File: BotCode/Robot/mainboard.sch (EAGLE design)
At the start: 18 parts

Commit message: UI improvements
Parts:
- renumbered HMC5883L_0 to HMC5883L, HMV5883L_1 to L3GD20H_LSM303
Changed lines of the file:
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@@
 <part name="GND6" library="SparkFun-Aesthetics" deviceset="GND" device=""/>
 <part name="GND7" library="SparkFun-Aesthetics" deviceset="GND" device=""/>
-<part name="HMV5883L_1" library="SparkFun-Connectors" deviceset="M04" device="PTH"/>
-<part name="HMC5883L_0" library="SparkFun-Connectors" deviceset="M04" device="PTH"/>
+<part name="L3GD20H_LSM303" library="SparkFun-Connectors" deviceset="M04" device="PTH"/>
+<part name="HMC5883L" library="SparkFun-Connectors" deviceset="M04" device="PTH"/>
 <part name="REGULATOR" library="LD1117V33" deviceset="LD1117V33" device=""/>
 <part name="LED_DRIVER" library="BillPorter" deviceset="TLC5916/17" device="DIP-16"/>
@@
 <instance part="GND6" gate="1" x="86.36" y="20.32"/>
 <instance part="GND7" gate="1" x="86.36" y="43.18"/>
-<instance part="HMV5883L_1" gate="G$1" x="119.38" y="58.42"/>
-<instance part="HMC5883L_0" gate="G$1" x="119.38" y="88.9"/>
+<instance part="L3GD20H_LSM303" gate="G$1" x="119.38" y="58.42"/>
+<instance part="HMC5883L" gate="G$1" x="119.38" y="88.9"/>
 <instance part="REGULATOR" gate="G$1" x="134.62" y="154.94"/>
 <instance part="LED_DRIVER" gate="G$1" x="88.9" y="109.22" rot="R180"/>
@@
 </segment>
 <segment>
-<pinref part="HMV5883L_1" gate="G$1" pin="2"/>
+<pinref part="L3GD20H_LSM303" gate="G$1" pin="2"/>
 <wire x1="124.46" y1="58.42" x2="132.08" y2="58.42" width="0.1524" layer="91"/>
 <pinref part="C2" gate="G$1" pin="1"/>
@@
 </segment>
 <segment>
-<pinref part="HMC5883L_0" gate="G$1" pin="2"/>
+<pinref part="HMC5883L" gate="G$1" pin="2"/>
 <wire x1="124.46" y1="88.9" x2="132.08" y2="88.9" width="0.1524" layer="91"/>
 <pinref part="C3" gate="G$1" pin="1"/>
@@
 <wire x1="149.86" y1="81.28" x2="144.78" y2="81.28" width="0.1524" layer="91"/>
 <wire x1="144.78" y1="81.28" x2="144.78" y2="93.98" width="0.1524" layer="91"/>
-<pinref part="HMC5883L_0" gate="G$1" pin="4"/>
+<pinref part="HMC5883L" gate="G$1" pin="4"/>
 <wire x1="144.78" y1="93.98" x2="124.46" y2="93.98" width="0.1524" layer="91"/>
 </segment>
@@
 <net name="N$17" class="0">
 <segment>
-<pinref part="HMC5883L_0" gate="G$1" pin="3"/>
+<pinref part="HMC5883L" gate="G$1" pin="3"/>
 <wire x1="124.46" y1="91.44" x2="142.24" y2="91.44" width="0.1524" layer="91"/>
 <wire x1="142.24" y1="91.44" x2="142.24" y2="78.74" width="0.1524" layer="91"/>
@@
 <wire x1="149.86" y1="68.58" x2="142.24" y2="68.58" width="0.1524" layer="91"/>
 <wire x1="142.24" y1="68.58" x2="142.24" y2="63.5" width="0.1524" layer="91"/>
-<pinref part="HMV5883L_1" gate="G$1" pin="4"/>
+<pinref part="L3GD20H_LSM303" gate="G$1" pin="4"/>
 <wire x1="142.24" y1="63.5" x2="124.46" y2="63.5" width="0.1524" layer="91"/>
 </segment>
@@
 <net name="N$21" class="0">
 <segment>
-<pinref part="HMV5883L_1" gate="G$1" pin="3"/>
+<pinref part="L3GD20H_LSM303" gate="G$1" pin="3"/>
 <wire x1="124.46" y1="60.96" x2="137.16" y2="60.96" width="0.1524" layer="91"/>
 <wire x1="137.16" y1="60.96" x2="137.16" y2="71.12" width="0.1524" layer="91"/>
@@
 </segment>
 <segment>
-<pinref part="HMV5883L_1" gate="G$1" pin="1"/>
+<pinref part="L3GD20H_LSM303" gate="G$1" pin="1"/>
 <wire x1="124.46" y1="55.88" x2="127" y2="55.88" width="0.1524" layer="91"/>
 <wire x1="127" y1="55.88" x2="127" y2="48.26" width="0.1524" layer="91"/>
@@
 </segment>
 <segment>
-<pinref part="HMC5883L_0" gate="G$1" pin="1"/>
+<pinref part="HMC5883L" gate="G$1" pin="1"/>
 <wire x1="124.46" y1="86.36" x2="127" y2="86.36" width="0.1524" layer="91"/>
 <wire x1="127" y1="86.36" x2="127" y2="78.74" width="0.1524" layer="91"/>

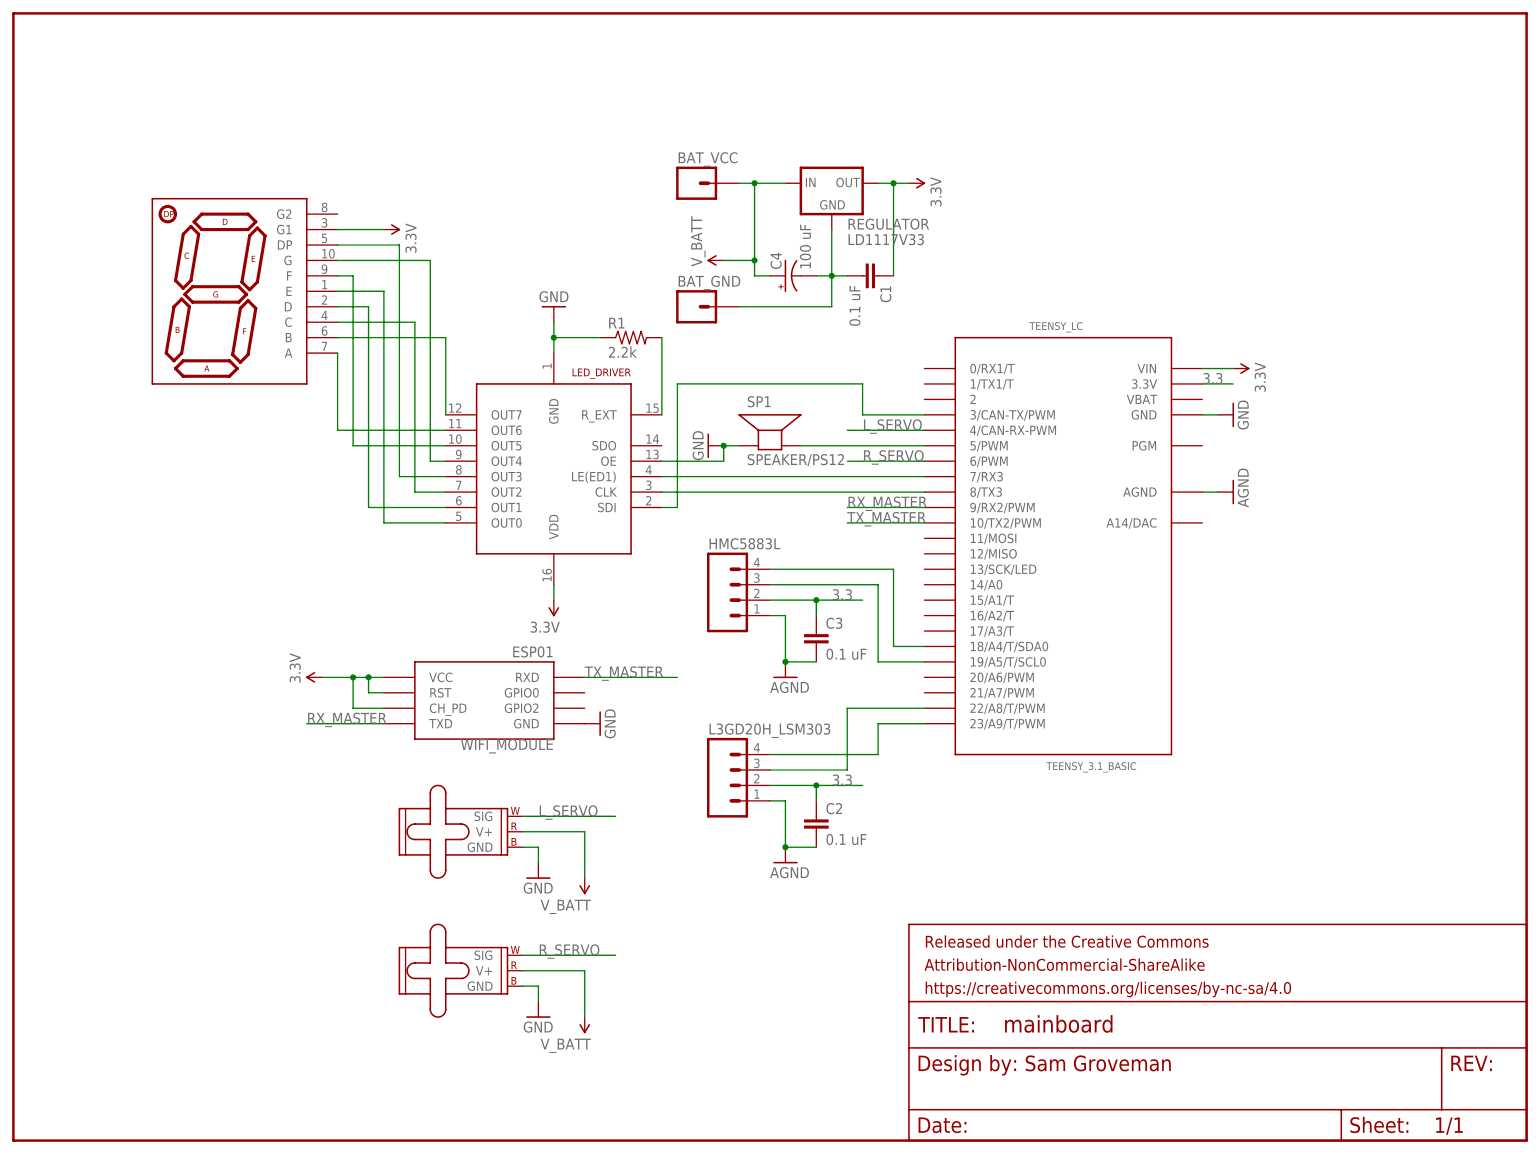
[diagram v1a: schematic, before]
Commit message: Added initial support for robot tuning.
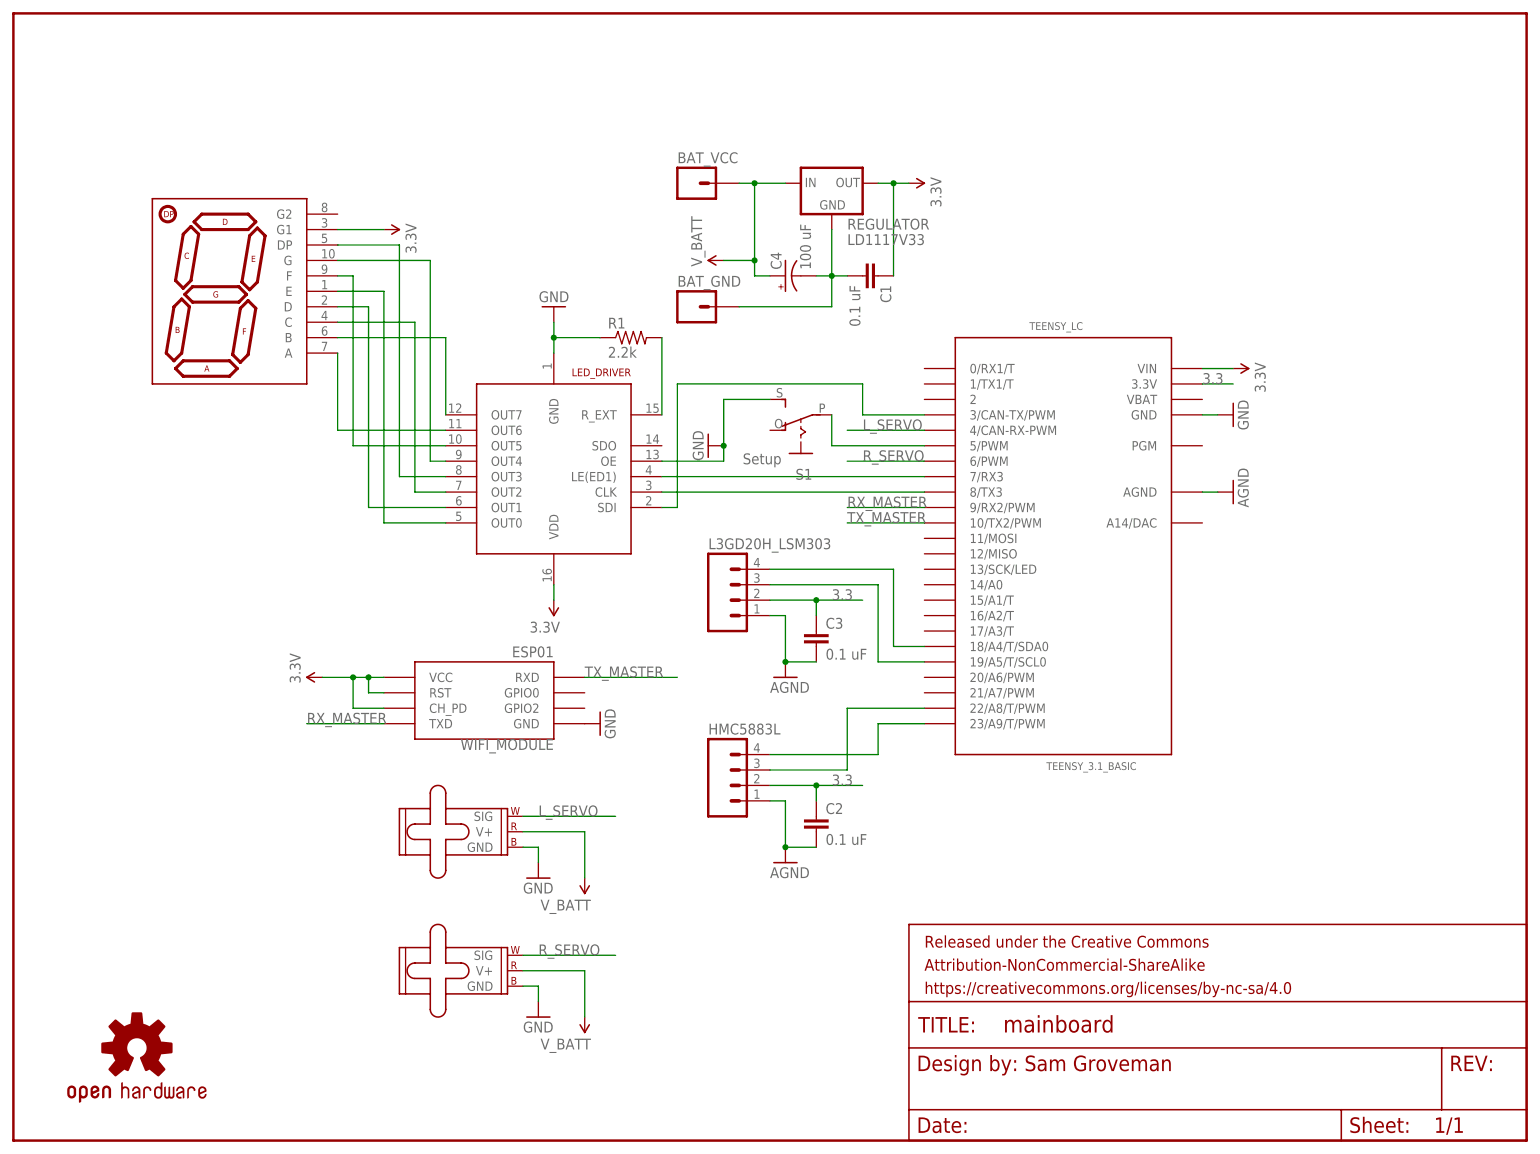
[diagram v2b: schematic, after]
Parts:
- removed SP1: SPEAKER/PS12, adafruit:SPEAKER/PS12
- added LOGO1: OSHW-LOGOL, SparkFun-Aesthetics:OSHW-LOGOL
- added S1: Setup, adafruit:EG1218S
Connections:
- net N$1 renamed R_EXT
- net N$10 renamed LED_4
- net N$11 renamed LED_9
- net N$12 renamed LED_10
- net N$2 renamed SDI
- net N$3 renamed CLK
- net N$4 renamed LE
- net N$5 renamed LED_5
- net N$6 renamed LED_6
- net N$7 renamed LED_1
- net N$8 renamed LED_2
- net N$9 renamed LED_7
- removed net N$15: SP1.-, TEENSY_LC.5/PWM
- removed net N$16: HMC5883L.4, TEENSY_LC.18/A4/T/SDA0
- removed net N$17: HMC5883L.3, TEENSY_LC.19/A5/T/SCL0
- removed net N$20: L3GD20H_LSM303.4, TEENSY_LC.23/A9/T/PWM
- removed net N$21: L3GD20H_LSM303.3, TEENSY_LC.22/A8/T/PWM
- new net F_SCL: HMC5883L.3, TEENSY_LC.22/A8/T/PWM
- new net F_SDA: HMC5883L.4, TEENSY_LC.23/A9/T/PWM
- new net R_SCL: L3GD20H_LSM303.3, TEENSY_LC.19/A5/T/SCL0
- new net R_SDA: L3GD20H_LSM303.4, TEENSY_LC.18/A4/T/SDA0
- new net SETUP: S1.P, TEENSY_LC.5/PWM
- net GND: now also S1.S; no longer SP1.+
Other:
- moved on the sheet: HMC5883L, L3GD20H_LSM303
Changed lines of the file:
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@@
 <?xml version="1.0" encoding="utf-8"?>
 <!DOCTYPE eagle SYSTEM "eagle.dtd">
-<eagle version="7.4.0">
+<eagle version="7.7.0">
 <drawing>
 <settings>
@@
 <setting verticaltext="up"/>
 </settings>
-<grid distance="0.1" unitdist="inch" unit="inch" style="lines" multiple="1" display="no" altdistance="0.01" altunitdist="inch" altunit="inch"/>
+<grid distance="0.1" unitdist="inch" unit="inch" style="lines" multiple="1" display="yes" altdistance="0.01" altunitdist="inch" altunit="inch"/>
 <layers>
 <layer number="1" name="Top" color="4" fill="1" visible="no" active="no"/>
@@
 <part name="C3" library="SparkFun-Passives" deviceset="CAP" device="PTH" value="0.1 uF"/>
 <part name="C4" library="SparkFun-Passives" deviceset="CAP_POL" device="PTH1" value="100 uF"/>
-<part name="SP1" library="adafruit" deviceset="SPEAKER" device="/PS12"/>
 <part name="R_SERVO" library="SparkFun-Electromechanical" deviceset="SMALL_SERVO" device=""/>
 <part name="L_SERVO" library="SparkFun-Electromechanical" deviceset="SMALL_SERVO" device=""/>
@@
 <part name="GND6" library="SparkFun-Aesthetics" deviceset="GND" device=""/>
 <part name="GND7" library="SparkFun-Aesthetics" deviceset="GND" device=""/>
+<part name="HMC5883L" library="SparkFun-Connectors" deviceset="M04" device="PTH"/>
 <part name="L3GD20H_LSM303" library="SparkFun-Connectors" deviceset="M04" device="PTH"/>
-<part name="HMC5883L" library="SparkFun-Connectors" deviceset="M04" device="PTH"/>
 <part name="REGULATOR" library="LD1117V33" deviceset="LD1117V33" device=""/>
 <part name="LED_DRIVER" library="BillPorter" deviceset="TLC5916/17" device="DIP-16"/>
@@
 <part name="SUPPLY7" library="SparkFun-Aesthetics" deviceset="V_BATT" device=""/>
 <part name="SUPPLY8" library="SparkFun-Aesthetics" deviceset="V_BATT" device=""/>
+<part name="LOGO1" library="SparkFun-Aesthetics" deviceset="OSHW-LOGO" device="L"/>
+<part name="S1" library="adafruit" deviceset="EG1218" device="S" value="Setup"/>
 </parts>
 <sheets>
@@
 <instance part="C3" gate="G$1" x="132.08" y="81.28"/>
 <instance part="C4" gate="G$1" x="127" y="142.24" rot="R90"/>
-<instance part="SP1" gate="S1" x="124.46" y="114.3"/>
 <instance part="R_SERVO" gate="G$1" x="81.28" y="30.48"/>
 <instance part="L_SERVO" gate="G$1" x="81.28" y="53.34"/>
@@
 <instance part="GND6" gate="1" x="86.36" y="20.32"/>
 <instance part="GND7" gate="1" x="86.36" y="43.18"/>
-<instance part="L3GD20H_LSM303" gate="G$1" x="119.38" y="58.42"/>
-<instance part="HMC5883L" gate="G$1" x="119.38" y="88.9"/>
+<instance part="HMC5883L" gate="G$1" x="119.38" y="58.42"/>
+<instance part="L3GD20H_LSM303" gate="G$1" x="119.38" y="88.9"/>
 <instance part="REGULATOR" gate="G$1" x="134.62" y="154.94"/>
 <instance part="LED_DRIVER" gate="G$1" x="88.9" y="109.22" rot="R180"/>
@@
 <instance part="SUPPLY7" gate="G$1" x="93.98" y="43.18" rot="R180"/>
 <instance part="SUPPLY8" gate="G$1" x="93.98" y="20.32" rot="R180"/>
+<instance part="LOGO1" gate="G$1" x="20.32" y="15.24"/>
+<instance part="S1" gate="1" x="129.54" y="116.84" rot="R90"/>
 </instances>
 <busses>
@@
 </segment>
 <segment>
-<pinref part="SP1" gate="S1" pin="+"/>
 <pinref part="GND5" gate="1" pin="GND"/>
-<wire x1="119.38" y1="114.3" x2="116.84" y2="114.3" width="0.1524" layer="91"/>
 <wire x1="106.68" y1="111.76" x2="116.84" y2="111.76" width="0.1524" layer="91"/>
 <wire x1="116.84" y1="111.76" x2="116.84" y2="114.3" width="0.1524" layer="91"/>
 <junction x="116.84" y="114.3"/>
 <pinref part="LED_DRIVER" gate="G$1" pin="OE"/>
+<wire x1="116.84" y1="114.3" x2="116.84" y2="121.92" width="0.1524" layer="91"/>
+<pinref part="S1" gate="1" pin="S"/>
+<wire x1="116.84" y1="121.92" x2="124.46" y2="121.92" width="0.1524" layer="91"/>
 </segment>
 <segment>
@@
 </segment>
 <segment>
-<pinref part="L3GD20H_LSM303" gate="G$1" pin="2"/>
+<pinref part="HMC5883L" gate="G$1" pin="2"/>
 <wire x1="124.46" y1="58.42" x2="132.08" y2="58.42" width="0.1524" layer="91"/>
 <pinref part="C2" gate="G$1" pin="1"/>
@@
 </segment>
 <segment>
-<pinref part="HMC5883L" gate="G$1" pin="2"/>
+<pinref part="L3GD20H_LSM303" gate="G$1" pin="2"/>
 <wire x1="124.46" y1="88.9" x2="132.08" y2="88.9" width="0.1524" layer="91"/>
 <pinref part="C3" gate="G$1" pin="1"/>
@@
 </segment>
 </net>
-<net name="N$1" class="0">
+<net name="R_EXT" class="0">
 <segment>
 <wire x1="106.68" y1="119.38" x2="106.68" y2="132.08" width="0.1524" layer="91"/>
@@
 </segment>
 </net>
-<net name="N$2" class="0">
+<net name="SDI" class="0">
 <segment>
 <wire x1="109.22" y1="124.46" x2="109.22" y2="104.14" width="0.1524" layer="91"/>
@@
 </segment>
 </net>
-<net name="N$3" class="0">
+<net name="CLK" class="0">
 <segment>
 <pinref part="TEENSY_LC" gate="G$1" pin="8/TX3"/>
@@
 </segment>
 </net>
-<net name="N$4" class="0">
+<net name="LE" class="0">
 <segment>
 <pinref part="TEENSY_LC" gate="G$1" pin="7/RX3"/>
@@
 </segment>
 </net>
-<net name="N$7" class="0">
+<net name="LED_1" class="0">
 <segment>
 <pinref part="U$4" gate="G$1" pin="E"/>
@@
 </segment>
 </net>
-<net name="N$8" class="0">
+<net name="LED_2" class="0">
 <segment>
 <pinref part="U$4" gate="G$1" pin="D"/>
@@
 </segment>
 </net>
-<net name="N$6" class="0">
+<net name="LED_6" class="0">
 <segment>
 <pinref part="U$4" gate="G$1" pin="B"/>
@@
 </segment>
 </net>
-<net name="N$9" class="0">
+<net name="LED_7" class="0">
 <segment>
 <pinref part="U$4" gate="G$1" pin="A"/>
@@
 </segment>
 </net>
-<net name="N$5" class="0">
+<net name="LED_5" class="0">
 <segment>
 <pinref part="U$4" gate="G$1" pin="DP"/>
@@
 </segment>
 </net>
-<net name="N$10" class="0">
+<net name="LED_4" class="0">
 <segment>
 <pinref part="U$4" gate="G$1" pin="C"/>
@@
 </segment>
 </net>
-<net name="N$11" class="0">
+<net name="LED_9" class="0">
 <segment>
 <pinref part="U$4" gate="G$1" pin="F"/>
@@
 </segment>
 </net>
-<net name="N$12" class="0">
+<net name="LED_10" class="0">
 <segment>
 <wire x1="71.12" y1="111.76" x2="68.58" y2="111.76" width="0.1524" layer="91"/>
@@
 </segment>
 </net>
-<net name="N$15" class="0">
-<segment>
-<pinref part="SP1" gate="S1" pin="-"/>
+<net name="SETUP" class="0">
+<segment>
 <pinref part="TEENSY_LC" gate="G$1" pin="5/PWM"/>
-<wire x1="129.54" y1="114.3" x2="149.86" y2="114.3" width="0.1524" layer="91"/>
+<wire x1="134.62" y1="114.3" x2="149.86" y2="114.3" width="0.1524" layer="91"/>
+<pinref part="S1" gate="1" pin="P"/>
+<wire x1="134.62" y1="119.38" x2="134.62" y2="114.3" width="0.1524" layer="91"/>
 </segment>
 </net>
@@
 </segment>
 </net>
-<net name="N$16" class="0">
+<net name="R_SDA" class="0">
 <segment>
 <pinref part="TEENSY_LC" gate="G$1" pin="18/A4/T/SDA0"/>
 <wire x1="149.86" y1="81.28" x2="144.78" y2="81.28" width="0.1524" layer="91"/>
 <wire x1="144.78" y1="81.28" x2="144.78" y2="93.98" width="0.1524" layer="91"/>
-<pinref part="HMC5883L" gate="G$1" pin="4"/>
+<pinref part="L3GD20H_LSM303" gate="G$1" pin="4"/>
 <wire x1="144.78" y1="93.98" x2="124.46" y2="93.98" width="0.1524" layer="91"/>
 </segment>
 </net>
-<net name="N$17" class="0">
-<segment>
-<pinref part="HMC5883L" gate="G$1" pin="3"/>
+<net name="R_SCL" class="0">
+<segment>
+<pinref part="L3GD20H_LSM303" gate="G$1" pin="3"/>
 <wire x1="124.46" y1="91.44" x2="142.24" y2="91.44" width="0.1524" layer="91"/>
 <wire x1="142.24" y1="91.44" x2="142.24" y2="78.74" width="0.1524" layer="91"/>
@@
 </segment>
 </net>
-<net name="N$20" class="0">
+<net name="F_SDA" class="0">
 <segment>
 <pinref part="TEENSY_LC" gate="G$1" pin="23/A9/T/PWM"/>
 <wire x1="149.86" y1="68.58" x2="142.24" y2="68.58" width="0.1524" layer="91"/>
 <wire x1="142.24" y1="68.58" x2="142.24" y2="63.5" width="0.1524" layer="91"/>
-<pinref part="L3GD20H_LSM303" gate="G$1" pin="4"/>
+<pinref part="HMC5883L" gate="G$1" pin="4"/>
 <wire x1="142.24" y1="63.5" x2="124.46" y2="63.5" width="0.1524" layer="91"/>
 </segment>
 </net>
-<net name="N$21" class="0">
-<segment>
-<pinref part="L3GD20H_LSM303" gate="G$1" pin="3"/>
+<net name="F_SCL" class="0">
+<segment>
+<pinref part="HMC5883L" gate="G$1" pin="3"/>
 <wire x1="124.46" y1="60.96" x2="137.16" y2="60.96" width="0.1524" layer="91"/>
 <wire x1="137.16" y1="60.96" x2="137.16" y2="71.12" width="0.1524" layer="91"/>
@@
 </segment>
 <segment>
-<pinref part="L3GD20H_LSM303" gate="G$1" pin="1"/>
+<pinref part="HMC5883L" gate="G$1" pin="1"/>
 <wire x1="124.46" y1="55.88" x2="127" y2="55.88" width="0.1524" layer="91"/>
 <wire x1="127" y1="55.88" x2="127" y2="48.26" width="0.1524" layer="91"/>
@@
 </segment>
 <segment>
-<pinref part="HMC5883L" gate="G$1" pin="1"/>
+<pinref part="L3GD20H_LSM303" gate="G$1" pin="1"/>
 <wire x1="124.46" y1="86.36" x2="127" y2="86.36" width="0.1524" layer="91"/>
 <wire x1="127" y1="86.36" x2="127" y2="78.74" width="0.1524" layer="91"/>
